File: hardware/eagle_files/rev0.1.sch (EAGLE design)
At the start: 64 parts, among them U1 AD8332ACPZ-R7, U2 AD8333ACPZ-REEL

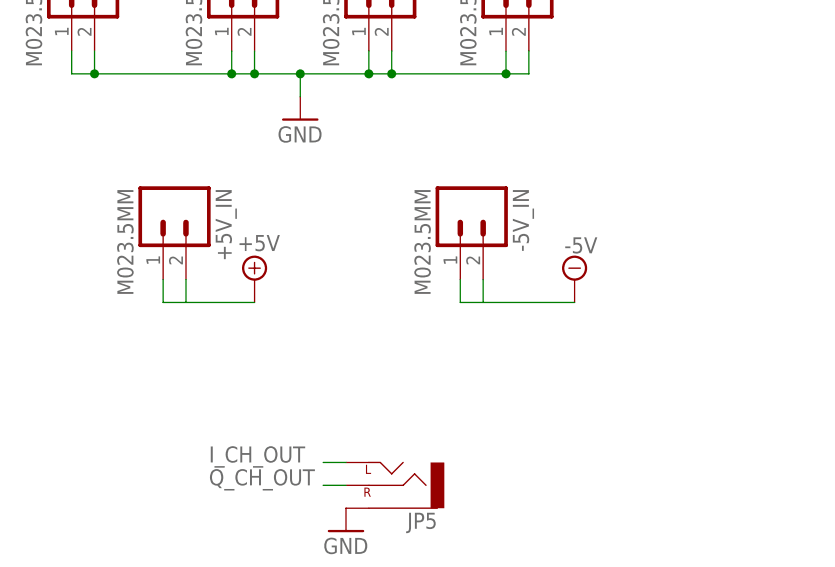
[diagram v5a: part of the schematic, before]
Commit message: Added tantalum caps to source input
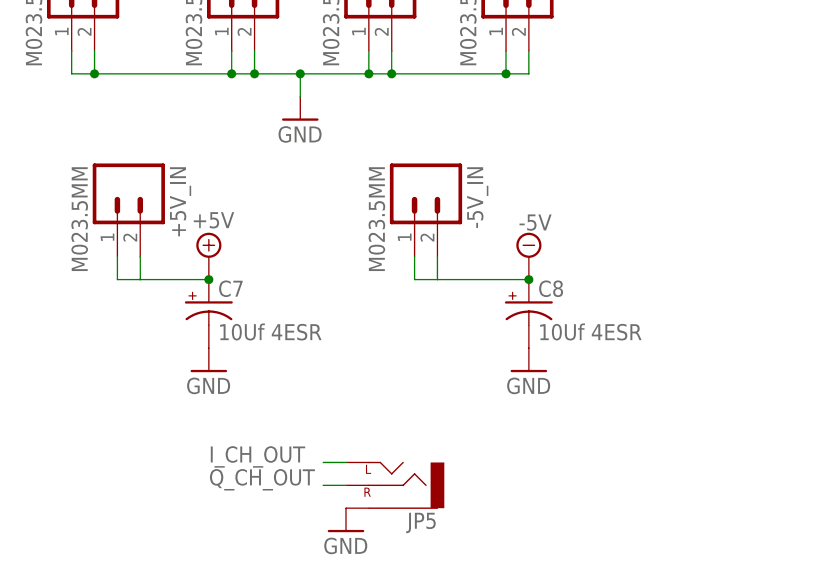
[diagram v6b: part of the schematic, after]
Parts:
- added C7, C8: 10Uf 4ESR, resistor:CPOL-USCT3216
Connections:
- net +5V: now also C7.+
- net -5V: now also C8.+
- net GND: now also C7.-, C8.-
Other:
- moved on the sheet: +5V_IN, -5V_IN
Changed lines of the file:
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@@
 <part name="JP6" library="SparkFun-Connectors" deviceset="AUDIO-JACK" device="PTH"/>
 <part name="GND32" library="supply1" deviceset="GND" device=""/>
+<part name="C7" library="resistor" deviceset="CPOL-US" device="CT3216" value="10Uf 4ESR"/>
+<part name="C8" library="resistor" deviceset="CPOL-US" device="CT3216" value="10Uf 4ESR"/>
+<part name="GND33" library="supply1" deviceset="GND" device=""/>
+<part name="GND34" library="supply1" deviceset="GND" device=""/>
 </parts>
 <sheets>
@@
 <instance part="JP3" gate="G$1" x="-71.12" y="193.04" rot="R270"/>
 <instance part="JP4" gate="G$1" x="-55.88" y="193.04" rot="R270"/>
-<instance part="+5V_IN" gate="G$1" x="-93.98" y="167.64" rot="R270"/>
-<instance part="-5V_IN" gate="G$1" x="-60.96" y="167.64" rot="R270"/>
+<instance part="+5V_IN" gate="G$1" x="-99.06" y="170.18" rot="R270"/>
+<instance part="-5V_IN" gate="G$1" x="-66.04" y="170.18" rot="R270"/>
 <instance part="GND29" gate="1" x="-78.74" y="177.8"/>
-<instance part="SUPPLY10" gate="+5V" x="-83.82" y="160.02"/>
-<instance part="SUPPLY11" gate="-5V" x="-48.26" y="160.02" rot="R180"/>
+<instance part="SUPPLY10" gate="+5V" x="-88.9" y="162.56"/>
+<instance part="SUPPLY11" gate="-5V" x="-53.34" y="162.56" rot="R180"/>
 <instance part="JP5" gate="G$1" x="-68.58" y="137.16" rot="R180"/>
 <instance part="GND31" gate="1" x="-73.66" y="132.08"/>
 <instance part="JP6" gate="G$1" x="-68.58" y="121.92" rot="R180"/>
 <instance part="GND32" gate="1" x="-73.66" y="116.84"/>
+<instance part="C7" gate="G$1" x="-88.9" y="157.48"/>
+<instance part="C8" gate="G$1" x="-53.34" y="157.48"/>
+<instance part="GND33" gate="1" x="-88.9" y="149.86"/>
+<instance part="GND34" gate="1" x="-53.34" y="149.86"/>
 </instances>
 <busses>
@@
 <pinref part="GND32" gate="1" pin="GND"/>
 </segment>
+<segment>
+<pinref part="C7" gate="G$1" pin="-"/>
+<pinref part="GND33" gate="1" pin="GND"/>
+</segment>
+<segment>
+<pinref part="C8" gate="G$1" pin="-"/>
+<pinref part="GND34" gate="1" pin="GND"/>
+</segment>
 </net>
 <net name="LMD1" class="0">
@@
 <segment>
 <pinref part="+5V_IN" gate="G$1" pin="1"/>
-<wire x1="-93.98" y1="160.02" x2="-93.98" y2="157.48" width="0.1524" layer="91"/>
+<wire x1="-99.06" y1="162.56" x2="-99.06" y2="160.02" width="0.1524" layer="91"/>
 <pinref part="+5V_IN" gate="G$1" pin="2"/>
-<wire x1="-93.98" y1="157.48" x2="-91.44" y2="157.48" width="0.1524" layer="91"/>
-<wire x1="-91.44" y1="157.48" x2="-91.44" y2="160.02" width="0.1524" layer="91"/>
-<wire x1="-91.44" y1="157.48" x2="-83.82" y2="157.48" width="0.1524" layer="91"/>
+<wire x1="-99.06" y1="160.02" x2="-96.52" y2="160.02" width="0.1524" layer="91"/>
+<wire x1="-96.52" y1="160.02" x2="-96.52" y2="162.56" width="0.1524" layer="91"/>
+<wire x1="-96.52" y1="160.02" x2="-88.9" y2="160.02" width="0.1524" layer="91"/>
 <pinref part="SUPPLY10" gate="+5V" pin="+5V"/>
+<pinref part="C7" gate="G$1" pin="+"/>
+<junction x="-88.9" y="160.02"/>
 </segment>
 </net>
@@
 <segment>
 <pinref part="-5V_IN" gate="G$1" pin="1"/>
-<wire x1="-60.96" y1="160.02" x2="-60.96" y2="157.48" width="0.1524" layer="91"/>
+<wire x1="-66.04" y1="162.56" x2="-66.04" y2="160.02" width="0.1524" layer="91"/>
 <pinref part="-5V_IN" gate="G$1" pin="2"/>
-<wire x1="-60.96" y1="157.48" x2="-58.42" y2="157.48" width="0.1524" layer="91"/>
-<wire x1="-58.42" y1="160.02" x2="-58.42" y2="157.48" width="0.1524" layer="91"/>
-<wire x1="-58.42" y1="157.48" x2="-48.26" y2="157.48" width="0.1524" layer="91"/>
+<wire x1="-66.04" y1="160.02" x2="-63.5" y2="160.02" width="0.1524" layer="91"/>
+<wire x1="-63.5" y1="162.56" x2="-63.5" y2="160.02" width="0.1524" layer="91"/>
+<wire x1="-63.5" y1="160.02" x2="-53.34" y2="160.02" width="0.1524" layer="91"/>
 <pinref part="SUPPLY11" gate="-5V" pin="-5V"/>
-</segment>
-</net>
+<pinref part="C8" gate="G$1" pin="+"/>
+<junction x="-53.34" y="160.02"/>
+</segment>
+</net>

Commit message: Issue 7 fixed: Changed C3 to C12
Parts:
- renumbered C3 to C12
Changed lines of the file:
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@@
 <part name="Z3" library="ds90c401" deviceset="DS90C401_D_8" device=""/>
 <part name="Z3_SPARE" library="ds90c401" deviceset="DS90C401_D_8" device=""/>
-<part name="C3" library="resistor" deviceset="C-US" device="C1206" value="0.1uF"/>
+<part name="C12" library="resistor" deviceset="C-US" device="C1206" value="0.1uF"/>
 <part name="C9" library="resistor" deviceset="C-US" device="C1206" value="0.1uF"/>
 <part name="GND10" library="supply1" deviceset="GND" device=""/>
@@
 <attribute name="VALUE" x="258.4958" y="-84.8614" size="2.0828" layer="96" ratio="6" rot="SR0"/>
 </instance>
-<instance part="C3" gate="G$1" x="231.14" y="-78.74" smashed="yes">
+<instance part="C12" gate="G$1" x="231.14" y="-78.74" smashed="yes">
 <attribute name="NAME" x="224.536" y="-78.105" size="1.778" layer="95"/>
 <attribute name="VALUE" x="224.536" y="-82.931" size="1.778" layer="96"/>
@@
 </segment>
 <segment>
-<pinref part="C3" gate="G$1" pin="2"/>
+<pinref part="C12" gate="G$1" pin="2"/>
 <pinref part="GND10" gate="1" pin="GND"/>
 </segment>
@@
 <segment>
 <pinref part="Z3_SPARE" gate="A" pin="VCC"/>
-<pinref part="C3" gate="G$1" pin="1"/>
+<pinref part="C12" gate="G$1" pin="1"/>
 <wire x1="238.76" y1="-76.2" x2="231.14" y2="-76.2" width="0.1524" layer="91"/>
 <pinref part="SUPPLY2" gate="+5V" pin="+5V"/>

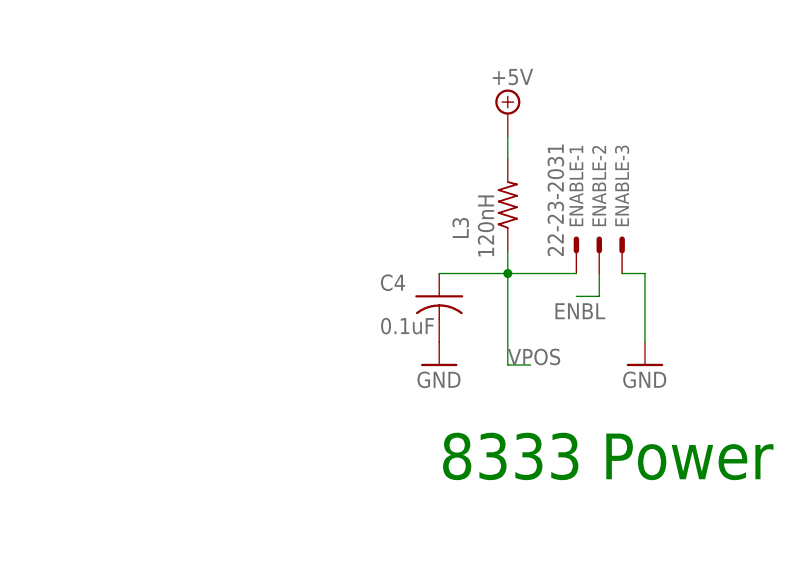
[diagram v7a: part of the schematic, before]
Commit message: Issue 12 fixed: Changed C4 to C24
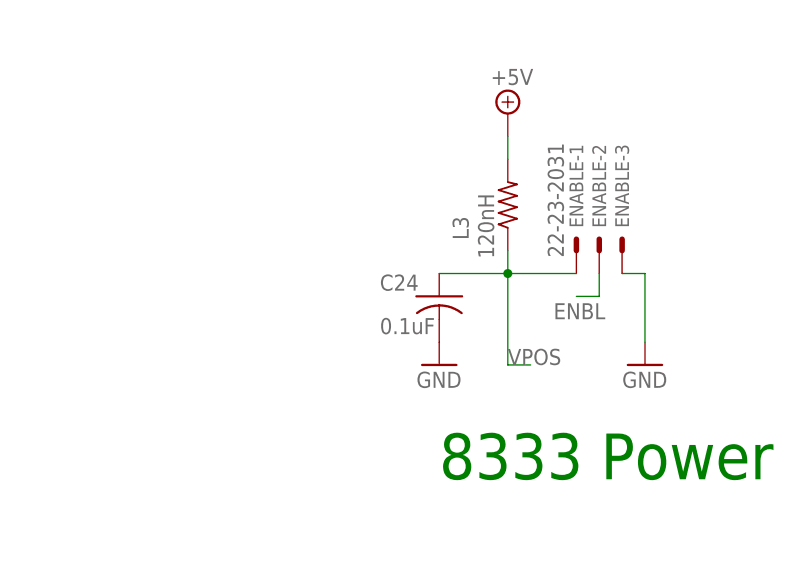
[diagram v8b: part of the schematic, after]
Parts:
- renumbered C4 to C24
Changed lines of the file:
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@@
 <part name="ENABLE" library="con-molex" deviceset="22-23-2031" device=""/>
 <part name="GND18" library="supply1" deviceset="GND" device=""/>
-<part name="C4" library="resistor" deviceset="C-US" device="C1206" value="0.1uF"/>
+<part name="C24" library="resistor" deviceset="C-US" device="C1206" value="0.1uF"/>
 <part name="GND19" library="supply1" deviceset="GND" device=""/>
 <part name="GND20" library="supply1" deviceset="GND" device=""/>
@@
 <instance part="ENABLE" gate="-3" x="149.86" y="182.88" rot="R90"/>
 <instance part="GND18" gate="1" x="152.4" y="170.18"/>
-<instance part="C4" gate="G$1" x="129.54" y="177.8" smashed="yes">
+<instance part="C24" gate="G$1" x="129.54" y="177.8" smashed="yes">
 <attribute name="NAME" x="122.936" y="178.435" size="1.778" layer="95"/>
 <attribute name="VALUE" x="122.936" y="173.609" size="1.778" layer="96"/>
@@
 </segment>
 <segment>
-<pinref part="C4" gate="G$1" pin="2"/>
+<pinref part="C24" gate="G$1" pin="2"/>
 <pinref part="GND19" gate="1" pin="GND"/>
 </segment>
@@
 <wire x1="137.16" y1="180.34" x2="137.16" y2="182.88" width="0.1524" layer="91"/>
 <junction x="137.16" y="180.34"/>
-<pinref part="C4" gate="G$1" pin="1"/>
+<pinref part="C24" gate="G$1" pin="1"/>
 <wire x1="129.54" y1="180.34" x2="137.16" y2="180.34" width="0.1524" layer="91"/>
 <wire x1="137.16" y1="180.34" x2="137.16" y2="170.18" width="0.1524" layer="91"/>
